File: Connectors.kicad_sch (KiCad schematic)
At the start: 10 parts, among them J1 282834-2, J2 200528-0100

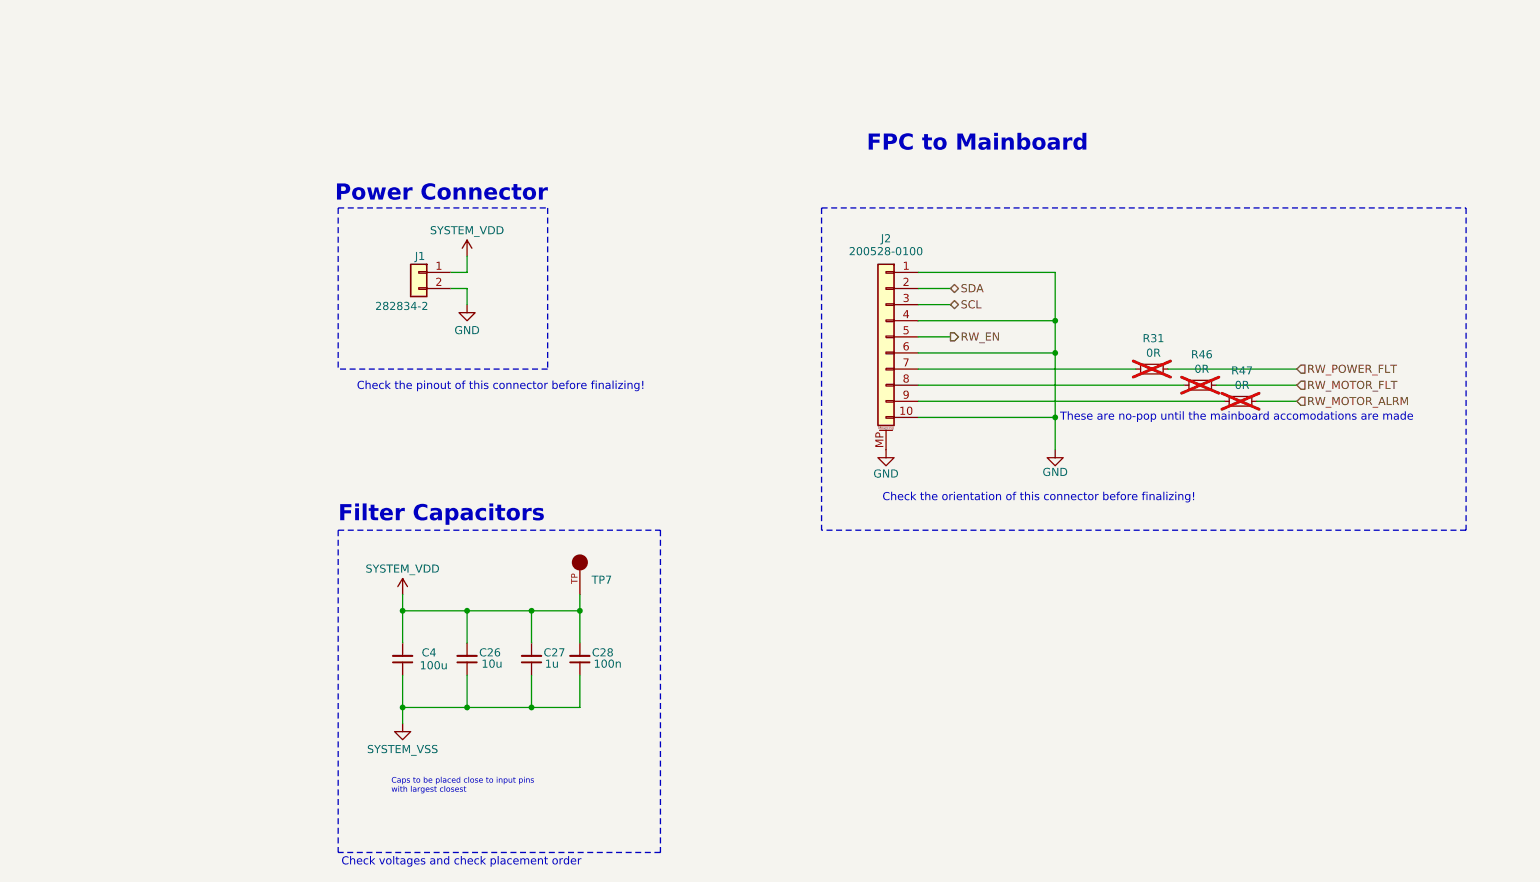
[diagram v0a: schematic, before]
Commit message: Checked all power and voltage ratings and corrected where needed. Still need footprints and layout completed.
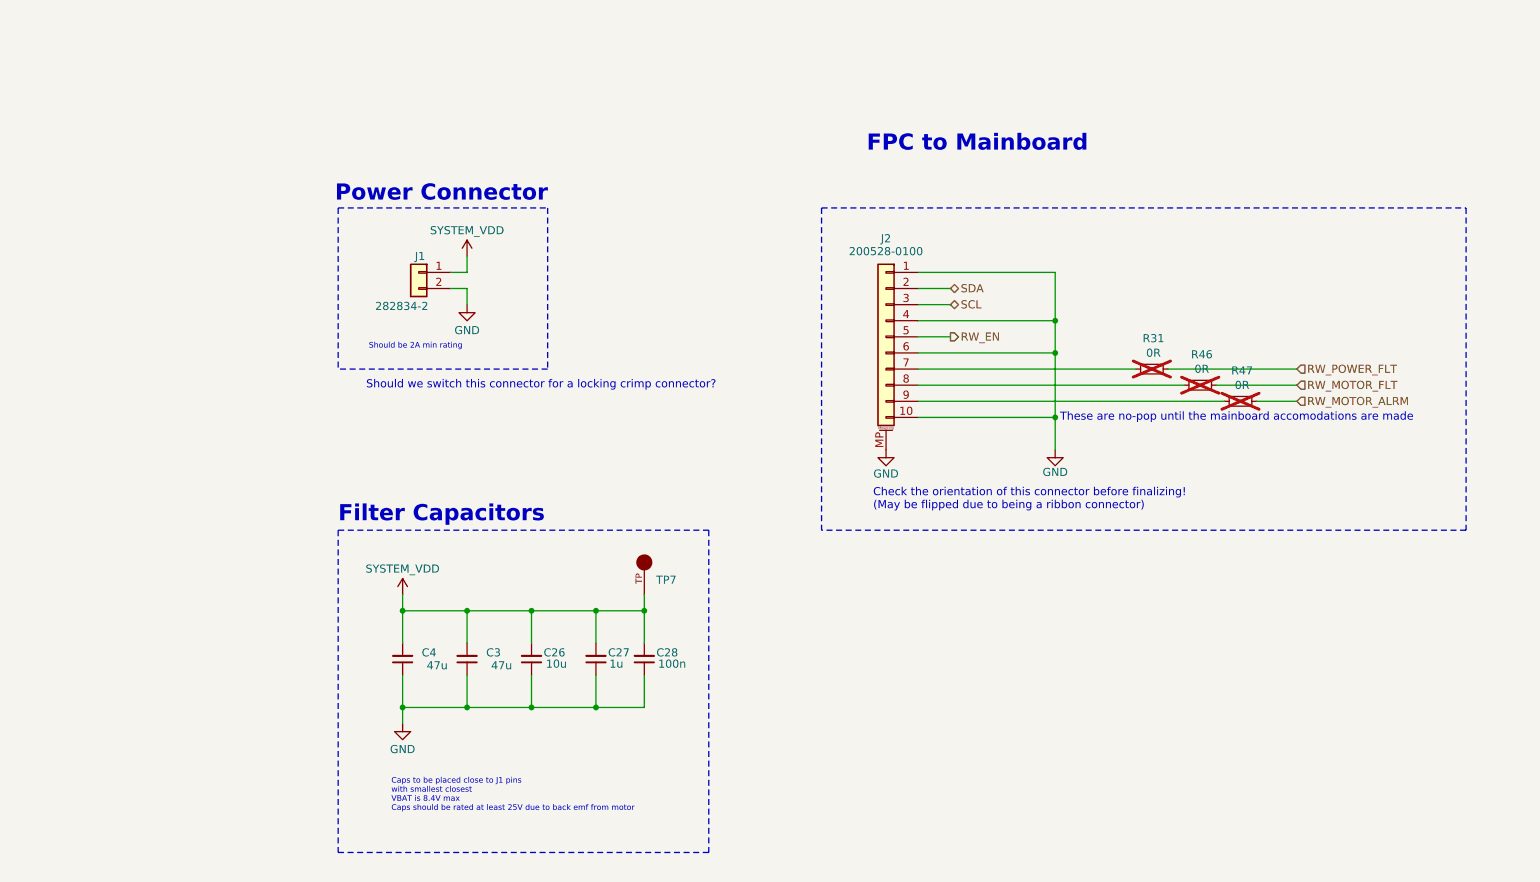
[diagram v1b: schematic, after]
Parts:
- added C3: 47u, Capacitor_SMD:C_1206_3216Metric_Pad1.33x1.80mm_HandSolder, symbol Device:C_Small
- C26: footprint Capacitor_SMD:C_0603_1608Metric -> Capacitor_SMD:C_1206_3216Metric_Pad1.33x1.80mm_HandSolder; Digikey (none) -> https://www.digikey.com/en/products/detail/samsung-electro-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; Part (none) -> CL31B106KAHNNNE
- C27: Digikey (none) -> https://www.digikey.com/en/products/detail/samsung-electro-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; Part (none) -> CL10B105KA8NNNC
- C28: footprint Capacitor_SMD:C_0603_1608Metric -> Capacitor_SMD:C_0402_1005Metric_Pad0.74x0.62mm_HandSolder; Digikey (none) -> https://www.digikey.com/en/products/detail/kemet/C0402C103K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; Part (none) -> C0402C103K3RACTU
- C4: value 100u -> 47u; footprint Capacitor_SMD:C_0603_1608Metric -> Capacitor_SMD:C_1206_3216Metric_Pad1.33x1.80mm_HandSolder; Digikey (none) -> https://www.digikey.com/en/products/detail/tdk-corporation/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; Part (none) -> C3216X5R1E476M160AC
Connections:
- net SYSTEM_VSS is gone; now on net GND: C26.1, C27.1, C28.1, C4.1
- net GND: now also C3.1
- net SYSTEM_VDD: now also C3.2
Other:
- note added: "Caps to be placed close to J1 pins with smallest closest VBAT is 8.4V max Caps should be rated at least 25V due to back emf from motor"
- note added: "Check the orientation of this connector before finalizing! (May be flipped due to being a ribbon connector)"
- note added: "Should be 2A min rating"
- note added: "Should we switch this connector for a locking crimp connector?"
- note removed: "Caps to be placed close to input pins with largest closest"
- note removed: "Check the orientation of this connector before finalizing!"
- note removed: "Check the pinout of this connector before finalizing!"
- note removed: "Check voltages and check placement order"
- moved on the sheet: C26, C27, C28, TP7

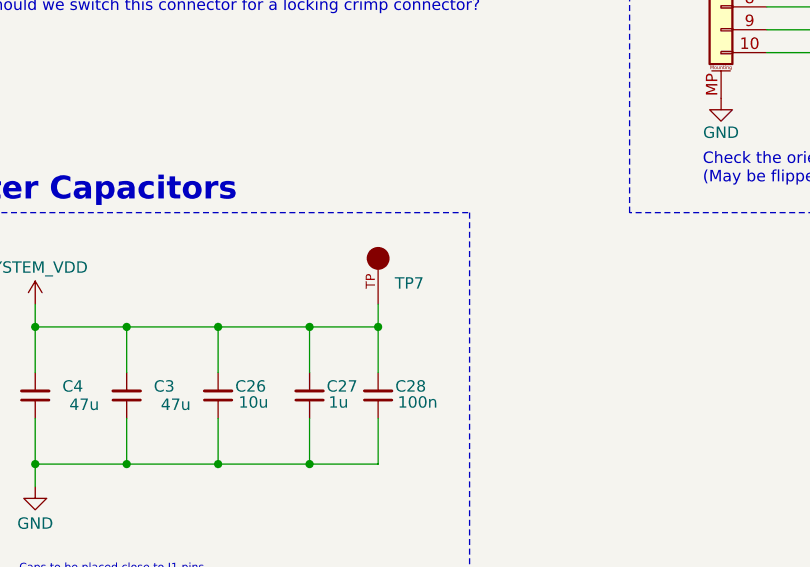
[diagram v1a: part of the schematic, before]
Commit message: Add more test points
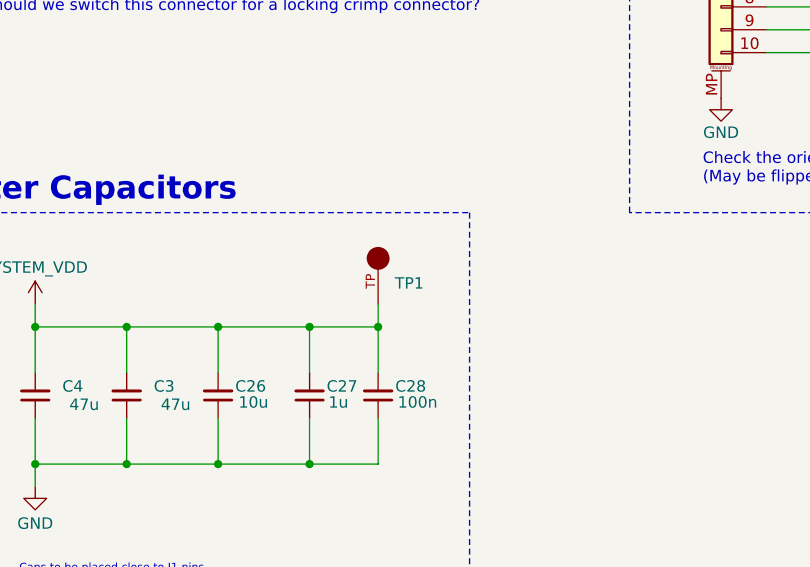
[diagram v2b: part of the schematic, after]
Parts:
- renumbered TP7 to TP1
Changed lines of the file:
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@@
 		(on_board yes)
 		(dnp no)
-		(property "Reference" "TP7"
+		(property "Reference" "TP1"
 			(at 129.54 108.712 90)
 			(do_not_autoplace yes)
@@
 			(project "Avionics-RWboard"
 				(path "/833dc880-24c2-430b-8cf7-cc984eb87a9d/e7579daf-9390-453f-be6d-47a1e5e63ac9"
-					(reference "TP7")
+					(reference "TP1")
 					(unit 1)
 				)

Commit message: Layout mostly complete
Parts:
- added C31, C36: 10uF, Capacitor_SMD:C_0603_1608Metric, symbol Device:C_Small
- added D8: ESD9X3.3ST5G, Diode_SMD:D_SOD-923, symbol Device:D_Zener_Filled
- added R18, R19: 0R, Resistor_SMD:R_0402_1005Metric_Pad0.72x0.64mm_HandSolder, symbol Device:R_Small
- added R51: 0R, Resistor_SMD:R_0603_1608Metric, symbol Device:R_Small
- added TP11: ~, Argus_RW_Library:KEYSTONE_5001, symbol Argus_RW_Library:5001
- added U3: NCP730BMT330TBG, WDFN6-2x2_511BR_OSI, symbol Argus_RW_Library:NCP730BMT330TBG
- R31, R46, R47: footprint Resistor_SMD:R_0603_1608Metric -> Resistor_SMD:R_0402_1005Metric_Pad0.72x0.64mm_HandSolder
- TP1: footprint (none) -> Argus_RW_Library:KEYSTONE_5001
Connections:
- net GND: now also C31.2, C36.2, D8.2 (A), U3.3 (GND), U3.7 (EPAD); no longer J2.1 (Pin_1)
- net SYSTEM_VDD renamed VMAIN
- new net +3V3: R18.1, R19.1
- new net 3V3_LDO: C36.1, R51.2, U3.1 (OUT)
- new net LOCAL_3V3: D8.1 (K), R19.2, R51.1, TP11.TP
- new net SYS_3V3: J2.1 (Pin_1), R18.2
- new net VM: C31.1, U3.4 (EN), U3.6 (IN)
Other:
- note added: "3.3V @150mA"
- note added: "3V3 For I2C Protection"
- note added: "Either R? or R? should be populated, but not both."
- note added: "I2C Power Selection"
- note added: "SYS_3V3 is not routed here on Mainboard at time of creating this board"
- note removed: "Should we switch this connector for a locking crimp connector?"
- title: (none) -> Argus Reaction Wheel
- moved on the sheet: C26, C27, C28, C3, C4, J1, J2, R31, TP1

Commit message: Add and correct BOM for easy Digikey ordering
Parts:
- C26: Digikey PN (none) -> 1276-1804-1-ND; MPN (none) -> CL31B106KAHNNNE
- C27: Digikey PN (none) -> 1276-1184-1-ND; MPN (none) -> CL10B105KA8NNNC
- C28: Digikey PN (none) -> 399-C0402C103K3RACTUCT-ND; MPN (none) -> C0402C103K3RACTU
- C3, C4: Digikey PN (none) -> 445-8047-1-ND; MPN (none) -> C3216X5R1E476M160AC
- C31: value 10uF -> 10u; Digikey (none) -> https://www.digikey.com/en/products/detail/tdk-corporation/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; Digikey PN (none) -> 445-9015-1-ND; Part (none) -> C1608X5R1E106M080AC
- C36: value 10uF -> 10u; Digikey (none) -> https://www.digikey.com/en/products/detail/tdk-corporation/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; Digikey PN (none) -> 445-9015-1-ND; MPN CC0402MRX5R5BB106 -> C1608X5R1E106M080AC; Part (none) -> C1608X5R1E106M080AC
- D8: Digikey (none) -> https://www.digikey.com/en/products/detail/onsemi/ESD9X3-3S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; Digikey PN (none) -> ESD9X3.3ST5GOSCT-ND; Part (none) -> ESD9X3.3ST5G
- J1: Digikey (none) -> https://www.digikey.com/en/products/detail/te-connectivity-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; Digikey PN (none) -> A98333-ND; MPN (none) -> 282834-2; Part (none) -> 282834-2
- J2: Digikey (none) -> https://www.digikey.com/en/products/detail/molex/2005280100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; Digikey PN (none) -> 900-2005280100CT-ND; MPN (none) -> 200528-0100; Part (none) -> 200528-0100
- R18, R19, R31, R46, R47: Digikey (none) -> https://www.digikey.com/en/products/detail/yageo/RC0402JR-0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; Digikey PN (none) -> 311-0.0JRCT-ND; MPN (none) -> RC0402JR-070RL; Part (none) -> RC0402JR-070RL
- R51: Digikey (none) -> https://www.digikey.com/en/products/detail/bourns-inc/CR060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; Digikey PN (none) -> CR0603-J/-000ELFCT-ND; Part (none) -> CR0603-J/-000ELF
- TP1, TP11: value ~ -> TP; Digikey (none) -> https://www.digikey.com/en/products/detail/keystone-electro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; Digikey PN (none) -> 36-5001-ND; MPN (none) -> 5001; Part (none) -> 5001
- U3: Digikey (none) -> https://www.digikey.com/en/products/detail/onsemi/NCP730BMT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; Digikey PN (none) -> 488-NCP730BMT330TBGCT-ND; MPN (none) -> NCP730BMT330TBG; Part (none) -> NCP730BMT330TBG

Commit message: Local Stash
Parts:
- J2: value 200528-0100 -> 522711069
